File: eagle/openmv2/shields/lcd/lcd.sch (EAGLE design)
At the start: 12 parts, among them J1 1X8, J2 1X8, Q1 MOSFET

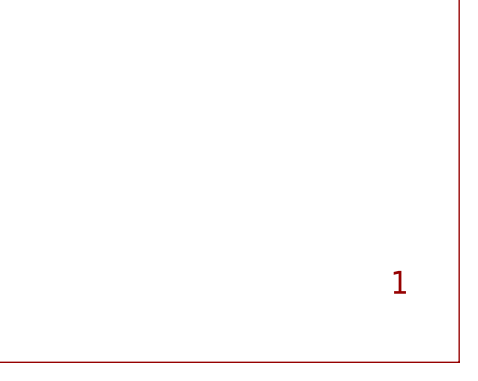
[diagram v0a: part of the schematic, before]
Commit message: Update shields silk-screen.
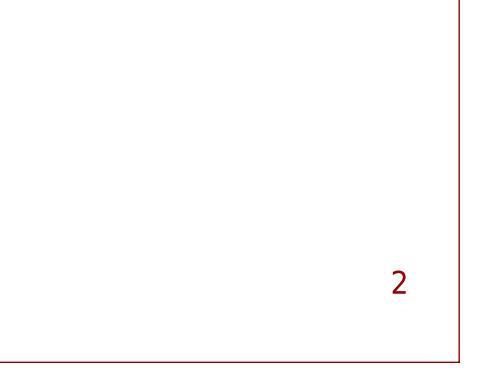
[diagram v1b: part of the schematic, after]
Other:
- note added: "2"
- note removed: "1"
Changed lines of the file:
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@@
 <text x="0" y="7.62" size="3.81" layer="150">This work is licensed under the Creative Commons Attribution-ShareAlike 3.0 License.</text>
 <text x="0" y="2.54" size="3.81" layer="150">To view a copy of this license, visit http://creativecommons.org/licenses/by-sa/3.0/</text>
-<text x="264.16" y="7.62" size="2.54" layer="94" ratio="12">1</text>
+<text x="264.16" y="7.62" size="2.54" layer="94" ratio="12">2</text>
 <wire x1="271.78" y1="167.64" x2="0" y2="167.64" width="0.1524" layer="94"/>
 <wire x1="0" y1="167.64" x2="0" y2="0" width="0.1524" layer="94"/>
